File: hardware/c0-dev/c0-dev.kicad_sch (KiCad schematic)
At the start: 0 parts

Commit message: schematic cleanup
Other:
- sheet Ethernet ports: added POE+12, POE+45, POE-36, POE-78; removed none
- sheet Power ports: added +3.3V_0, +3.3V_1, +3.3V_2, +5V_0, +5V_1, +5V_2, GND_0, GND_1, GND_2, POE+12, POE+45, POE-36, POE-78, T2P; removed none
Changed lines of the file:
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@@
 	(generator_version "10.0")
 	(paper "A4")
+	(wire
+		(pts
+			(xy 50.8 48.26) (xy 76.2 48.26)
+		)
+		(stroke
+			(width 0)
+			(type default)
+		)
+	)
+	(wire
+		(pts
+			(xy 50.8 40.64) (xy 76.2 40.64)
+		)
+		(stroke
+			(width 0)
+			(type default)
+		)
+	)
+	(wire
+		(pts
+			(xy 50.8 43.18) (xy 76.2 43.18)
+		)
+		(stroke
+			(width 0)
+			(type default)
+		)
+	)
+	(wire
+		(pts
+			(xy 50.8 45.72) (xy 76.2 45.72)
+		)
+		(stroke
+			(width 0)
+			(type default)
+		)
+	)
 	(sheet
-		(at 38.1 76.2)
-		(size 25.4 12.7)
+		(at 76.2 38.1)
+		(size 25.4 38.1)
 		(exclude_from_sim no)
 		(in_bom yes)
@@
 		)
 		(property "Sheetname" "Power"
-			(at 38.1 75.4884 0)
+			(at 76.2 37.3884 0)
 			(show_name no)
 			(do_not_autoplace no)
@@
 		)
 		(property "Sheetfile" "power.kicad_sch"
-			(at 38.1 89.4846 0)
+			(at 76.2 76.7846 0)
 			(show_name no)
 			(do_not_autoplace no)
@@
 				)
 				(justify left top)
+			)
+		)
+		(pin "+3.3V_0" passive
+			(at 101.6 40.64 0)
+			(effects
+				(font
+					(size 1.27 1.27)
+				)
+				(justify right)
+			)
+		)
+		(pin "+3.3V_1" passive
+			(at 101.6 50.8 0)
+			(effects
+				(font
+					(size 1.27 1.27)
+				)
+				(justify right)
+			)
+		)
+		(pin "+3.3V_2" passive
+			(at 101.6 62.23 0)
+			(effects
+				(font
+					(size 1.27 1.27)
+				)
+				(justify right)
+			)
+		)
+		(pin "+5V_0" passive
+			(at 101.6 43.18 0)
+			(effects
+				(font
+					(size 1.27 1.27)
+				)
+				(justify right)
+			)
+		)
+		(pin "+5V_1" passive
+			(at 101.6 53.34 0)
+			(effects
+				(font
+					(size 1.27 1.27)
+				)
+				(justify right)
+			)
+		)
+		(pin "+5V_2" passive
+			(at 101.6 64.77 0)
+			(effects
+				(font
+					(size 1.27 1.27)
+				)
+				(justify right)
+			)
+		)
+		(pin "GND_0" passive
+			(at 101.6 45.72 0)
+			(effects
+				(font
+					(size 1.27 1.27)
+				)
+				(justify right)
+			)
+		)
+		(pin "GND_1" passive
+			(at 101.6 55.88 0)
+			(effects
+				(font
+					(size 1.27 1.27)
+				)
+				(justify right)
+			)
+		)
+		(pin "GND_2" passive
+			(at 101.6 67.31 0)
+			(effects
+				(font
+					(size 1.27 1.27)
+				)
+				(justify right)
+			)
+		)
+		(pin "POE+12" input
+			(at 76.2 40.64 180)
+			(effects
+				(font
+					(size 1.27 1.27)
+				)
+				(justify left)
+			)
+		)
+		(pin "POE+45" input
+			(at 76.2 43.18 180)
+			(effects
+				(font
+					(size 1.27 1.27)
+				)
+				(justify left)
+			)
+		)
+		(pin "POE-36" input
+			(at 76.2 45.72 180)
+			(effects
+				(font
+					(size 1.27 1.27)
+				)
+				(justify left)
+			)
+		)
+		(pin "POE-78" input
+			(at 76.2 48.26 180)
+			(effects
+				(font
+					(size 1.27 1.27)
+				)
+				(justify left)
+			)
+		)
+		(pin "T2P" output
+			(at 101.6 73.66 0)
+			(effects
+				(font
+					(size 1.27 1.27)
+				)
+				(justify right)
 			)
 		)
@@
 	(sheet
 		(at 38.1 38.1)
-		(size 25.4 25.4)
+		(size 12.7 152.4)
 		(exclude_from_sim no)
 		(in_bom yes)
@@
 		)
 		(property "Sheetfile" "ethernet.kicad_sch"
-			(at 38.1 64.0846 0)
+			(at 38.1 191.0846 0)
 			(show_name no)
 			(do_not_autoplace no)
@@
 				)
 				(justify left top)
+			)
+		)
+		(pin "POE+12" input
+			(at 50.8 40.64 0)
+			(effects
+				(font
+					(size 1.27 1.27)
+				)
+				(justify right)
+			)
+		)
+		(pin "POE+45" input
+			(at 50.8 43.18 0)
+			(effects
+				(font
+					(size 1.27 1.27)
+				)
+				(justify right)
+			)
+		)
+		(pin "POE-36" input
+			(at 50.8 45.72 0)
+			(effects
+				(font
+					(size 1.27 1.27)
+				)
+				(justify right)
+			)
+		)
+		(pin "POE-78" input
+			(at 50.8 48.26 0)
+			(effects
+				(font
+					(size 1.27 1.27)
+				)
+				(justify right)
 			)
 		)
@@
 	)
 	(sheet
-		(at 38.1 101.6)
-		(size 25.4 25.4)
+		(at 76.2 127)
+		(size 25.4 63.5)
 		(exclude_from_sim no)
 		(in_bom yes)
@@
 		)
 		(property "Sheetname" "MCU"
-			(at 38.1 100.8884 0)
+			(at 76.2 126.2884 0)
 			(show_name no)
 			(do_not_autoplace no)
@@
 		)
 		(property "Sheetfile" "mcu.kicad_sch"
-			(at 38.1 127.5846 0)
-			(show_name no)
-			(do_not_autoplace no)
+			(at 76.2 191.0846 0)
+			(show_name no)
+			(do_not_autoplace no)

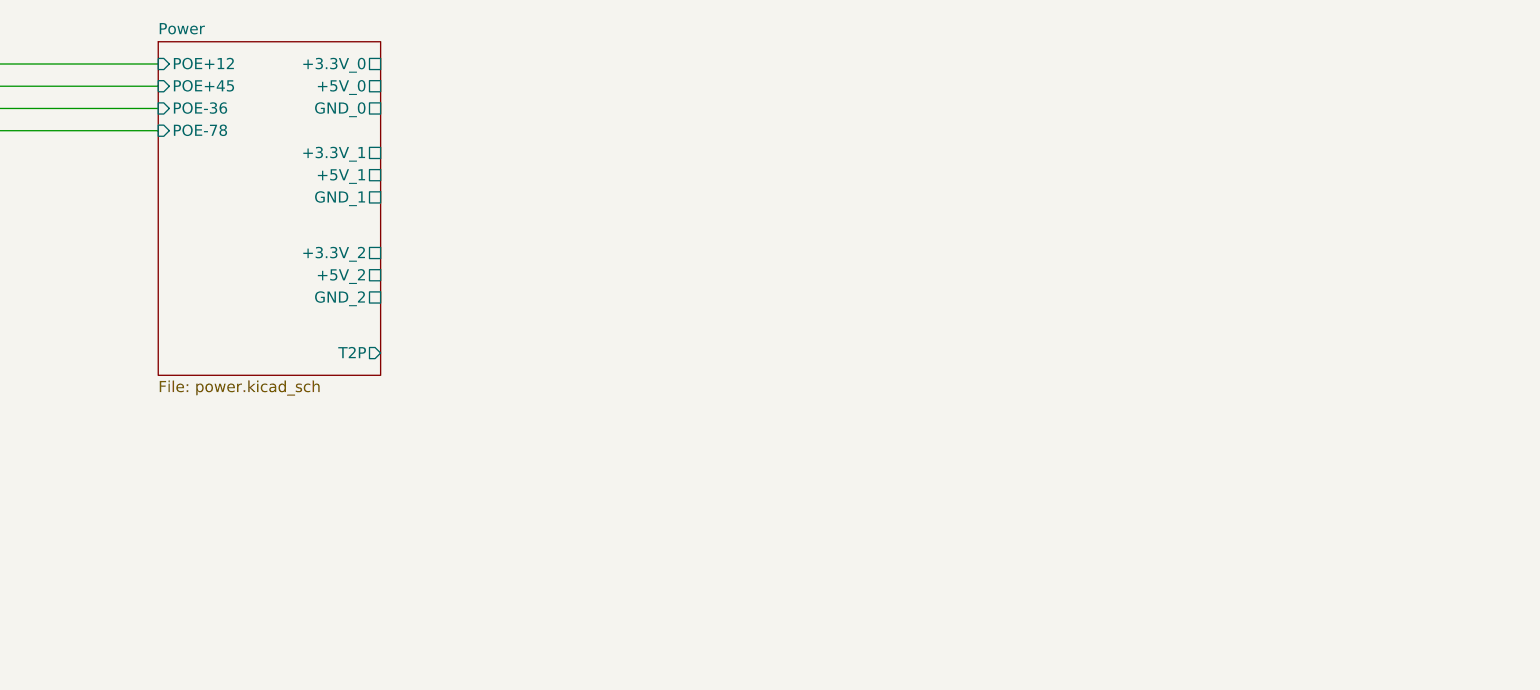
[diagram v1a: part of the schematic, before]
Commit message: added frontend + selected adc
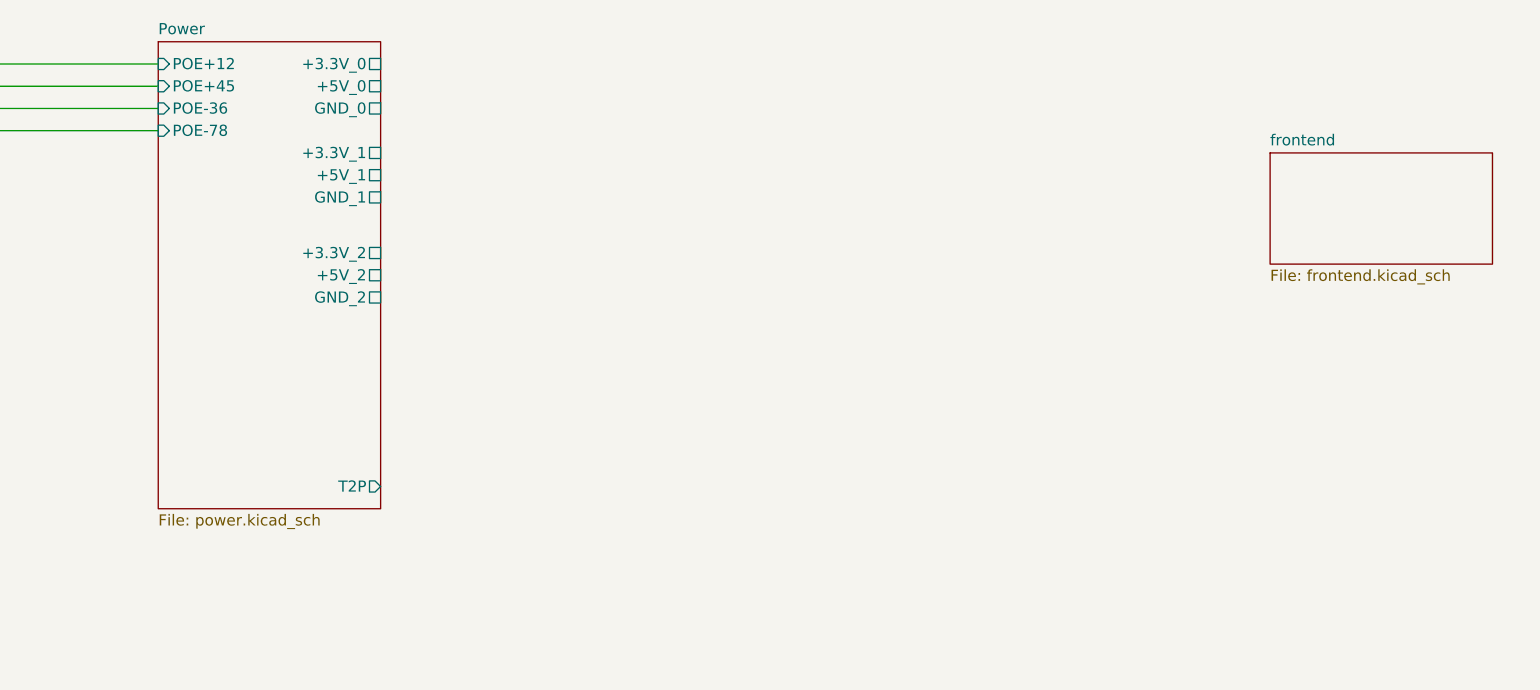
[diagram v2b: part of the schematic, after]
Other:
- added sheet frontend (frontend.kicad_sch)
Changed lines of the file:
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@@
 	(sheet
 		(at 76.2 38.1)
-		(size 25.4 38.1)
+		(size 25.4 53.34)
 		(exclude_from_sim no)
 		(in_bom yes)
@@
 		)
 		(property "Sheetfile" "power.kicad_sch"
-			(at 76.2 76.7846 0)
+			(at 76.2 92.0246 0)
 			(show_name no)
 			(do_not_autoplace no)
@@
 		)
 		(pin "T2P" output
-			(at 101.6 73.66 0)
+			(at 101.6 88.9 0)
 			(effects
 				(font
@@
 				)
 			)
+		)
+	)
+	(sheet
+		(at 203.2 50.8)
+		(size 25.4 12.7)
+		(exclude_from_sim no)
+		(in_bom yes)
+		(on_board yes)
+		(dnp no)
+		(fields_autoplaced yes)
+		(stroke
+			(width 0.1524)
+			(type solid)
+		)
+		(fill
+			(color 0 0 0 0)
+		)
+		(property "Sheetname" "frontend"
+			(at 203.2 50.0884 0)
+			(show_name no)
+			(do_not_autoplace no)
+			(effects
+				(font
+					(size 1.27 1.27)
+				)
+				(justify left bottom)
+			)
+		)
+		(property "Sheetfile" "frontend.kicad_sch"
+			(at 203.2 64.0846 0)
+			(show_name no)
+			(do_not_autoplace no)
+			(effects
+				(font
+					(size 1.27 1.27)
+				)
+				(justify left top)
+			)
+		)
+		(instances
+			(project "c0-dev"
+				(path "/b8347a0e-ad04-4414-969d-3c64a611d74e"
+					(page "5")
+				)
+			)

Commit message: schematic structure
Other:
- sheet Ethernet ports: added CLK, MDIO0{MDIO MDC}, RMII{TXD0 TXD1 TXEN RXD0 RXD1 CRS}, ~{RST}; removed none
- sheet Power ports: added none; removed +3.3V_0, +3.3V_1, +3.3V_2, +5V_0, +5V_1, +5V_2, GND_0, GND_1, GND_2
- sheet frontend ports: added +5V, +5V_ISO, ADDR, AIN0, AIN1, AIN2, AIN3, GND, GND_ISO, SCL, SDA; removed none

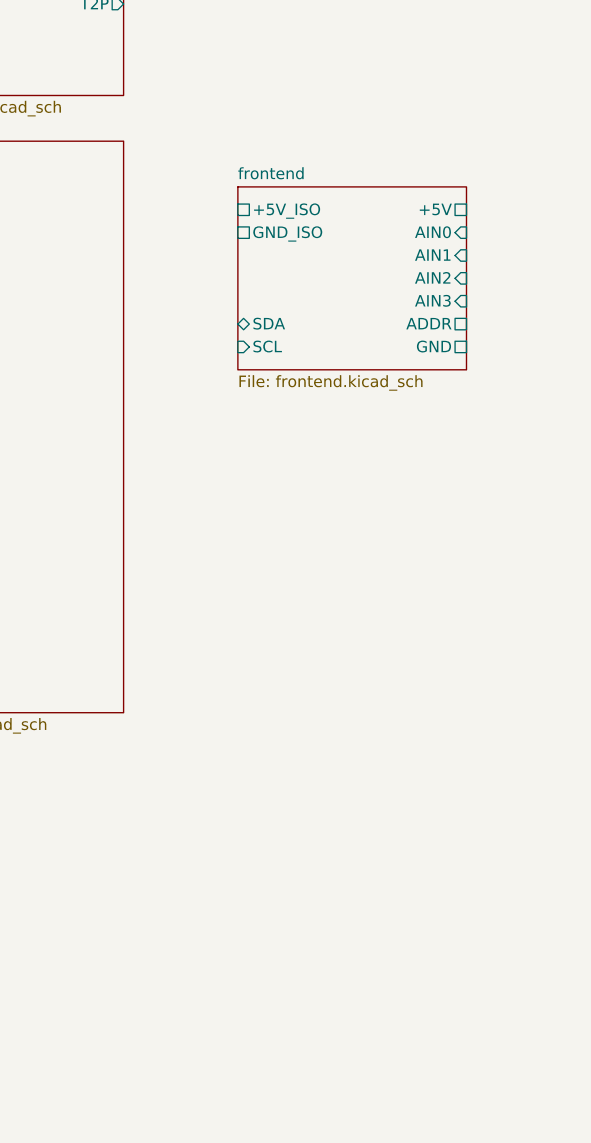
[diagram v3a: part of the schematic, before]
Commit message: added protection to tc inputs
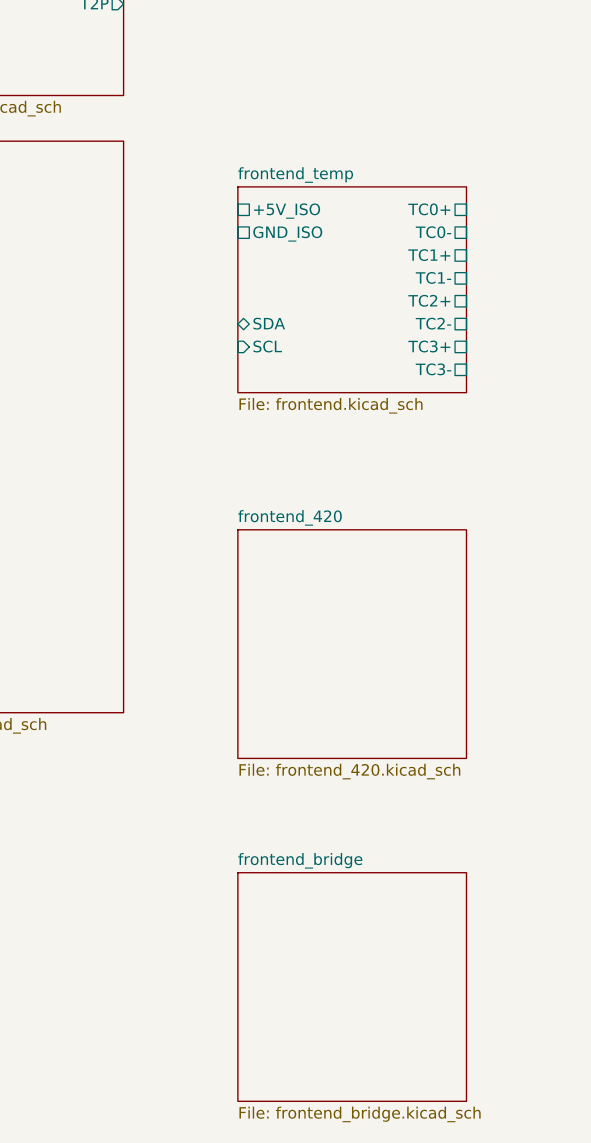
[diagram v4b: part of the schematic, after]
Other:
- sheet frontend renamed frontend_temp
- added sheet frontend_420 (frontend_420.kicad_sch)
- added sheet frontend_bridge (frontend_bridge.kicad_sch)
- sheet frontend_temp ports: added TC0+, TC0-, TC1+, TC1-, TC2+, TC2-, TC3+, TC3-; removed +5V, ADDR, AIN0, AIN1, AIN2, AIN3, GND
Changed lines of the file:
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@@
+	)
+	(sheet
+		(at 127 88.9)
+		(size 25.4 25.4)
+		(exclude_from_sim no)
+		(in_bom yes)
+		(on_board yes)
+		(dnp no)
+		(fields_autoplaced yes)
+		(stroke
+			(width 0.1524)
+			(type solid)
+		)
+		(fill
+			(color 0 0 0 0)
+		)
+		(property "Sheetname" "frontend_420"
+			(at 127 88.1884 0)
+			(show_name no)
+			(do_not_autoplace no)
+			(effects
+				(font
+					(size 1.27 1.27)
+				)
+				(justify left bottom)
+			)
+		)
+		(property "Sheetfile" "frontend_420.kicad_sch"
+			(at 127 114.8846 0)
+			(show_name no)
+			(do_not_autoplace no)
+			(effects
+				(font
+					(size 1.27 1.27)
+				)
+				(justify left top)
+			)
+		)
+		(instances
+			(project "c0-dev"
+				(path "/b8347a0e-ad04-4414-969d-3c64a611d74e"
+					(page "6")
+				)
+			)
+		)
 	)
 	(sheet
@@
 	(sheet
 		(at 127 50.8)
-		(size 25.4 20.32)
+		(size 25.4 22.86)
 		(exclude_from_sim no)
 		(in_bom yes)
@@
 			(color 0 0 0 0)
 		)
-		(property "Sheetname" "frontend"
+		(property "Sheetname" "frontend_temp"
 			(at 127 50.0884 0)
 			(show_name no)
@@
 		)
 		(property "Sheetfile" "frontend.kicad_sch"
-			(at 127 71.7046 0)
+			(at 127 74.2446 0)
 			(show_name no)
 			(do_not_autoplace no)
@@
 			)
 		)
-		(pin "AIN1" input
+		(pin "TC1+" passive
 			(at 152.4 58.42 0)
 			(effects
@@
 			)
 		)
-		(pin "ADDR" passive
+		(pin "TC0-" passive
+			(at 152.4 55.88 0)
+			(effects
+				(font
+					(size 1.27 1.27)
+				)
+				(justify right)
+			)
+		)
+		(pin "TC1-" passive
+			(at 152.4 60.96 0)
+			(effects
+				(font
+					(size 1.27 1.27)
+				)
+				(justify right)
+			)
+		)
+		(pin "TC0+" passive
+			(at 152.4 53.34 0)
+			(effects
+				(font
+					(size 1.27 1.27)
+				)
+				(justify right)
+			)
+		)
+		(pin "TC2+" passive
+			(at 152.4 63.5 0)
+			(effects
+				(font
+					(size 1.27 1.27)
+				)
+				(justify right)
+			)
+		)
+		(pin "TC3+" passive
+			(at 152.4 68.58 0)
+			(effects
+				(font
+					(size 1.27 1.27)
+				)
+				(justify right)
+			)
+		)
+		(pin "TC2-" passive
 			(at 152.4 66.04 0)
 			(effects
@@
 			)
 		)
-		(pin "AIN0" input
-			(at 152.4 55.88 0)
-			(effects
-				(font
-					(size 1.27 1.27)
-				)
-				(justify right)
-			)
-		)
-		(pin "AIN2" input
-			(at 152.4 60.96 0)
-			(effects
-				(font
-					(size 1.27 1.27)
-				)
-				(justify right)
-			)
-		)
-		(pin "AIN3" input
-			(at 152.4 63.5 0)
-			(effects
-				(font
-					(size 1.27 1.27)
-				)
-				(justify right)
-			)
-		)
-		(pin "GND" passive
-			(at 152.4 68.58 0)
-			(effects
-				(font
-					(size 1.27 1.27)
-				)
-				(justify right)
-			)
-		)
-		(pin "+5V" passive
-			(at 152.4 53.34 0)
+		(pin "TC3-" passive
+			(at 152.4 71.12 0)
 			(effects
 				(font
@@
 				)
 			)
+		)
+	)
+	(sheet
+		(at 127 127)
+		(size 25.4 25.4)
+		(exclude_from_sim no)
+		(in_bom yes)
+		(on_board yes)
+		(dnp no)
+		(fields_autoplaced yes)
+		(stroke
+			(width 0.1524)
+			(type solid)
+		)
+		(fill
+			(color 0 0 0 0)
+		)
+		(property "Sheetname" "frontend_bridge"
+			(at 127 126.2884 0)
+			(show_name no)
+			(do_not_autoplace no)
+			(effects
+				(font
+					(size 1.27 1.27)
+				)
+				(justify left bottom)
+			)
+		)
+		(property "Sheetfile" "frontend_bridge.kicad_sch"
+			(at 127 152.9846 0)
+			(show_name no)
+			(do_not_autoplace no)
+			(effects
+				(font
+					(size 1.27 1.27)
+				)
+				(justify left top)
+			)
+		)
+		(instances
+			(project "c0-dev"
+				(path "/b8347a0e-ad04-4414-969d-3c64a611d74e"
+					(page "7")
+				)
+			)

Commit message: interface clanup and CAN
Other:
- added sheet CAN (can.kicad_sch)
- sheet MCU ports: added LANCLK; removed none
- sheet frontend_420 ports: added +5V_ISO, 4200, 4201, 4202, 4203, 420_GND, GND_ISO, SCL, SDA; removed none
- sheet frontend_bridge ports: added +5V_ISO, B0+, B0-, B0_5V+, B0_GND, B1+, B1-, B1_5V+, B1_GND, CLK_ISO, DIN_ISO, DOUT_ISO, GND_ISO, ~{CS0_ISO}, ~{CS1_ISO}; removed none
